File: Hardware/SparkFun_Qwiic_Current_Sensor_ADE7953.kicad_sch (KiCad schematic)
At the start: 45 parts, among them J1 Qwiic_RA, J2 Qwiic_RA, J3 Conn_01x06, J4 Conn_01x02, J5 3.5mm TRRS, J6 Conn_01x02, U1 ADE7953ACPZ, Y1 3.579545MHz

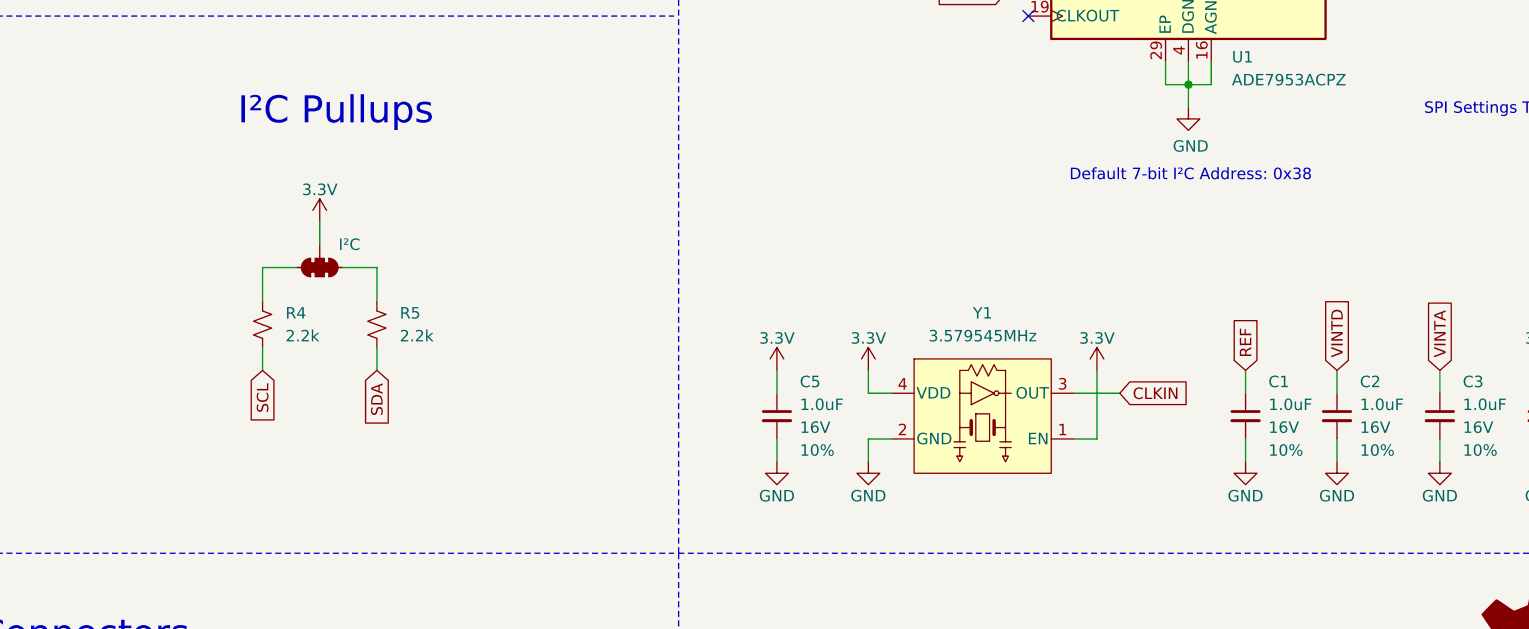
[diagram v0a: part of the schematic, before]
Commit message: Updated PCB based on Design Review II feedback
- Updated schematic I2C labels
- Updated component silkscreens and courtyards
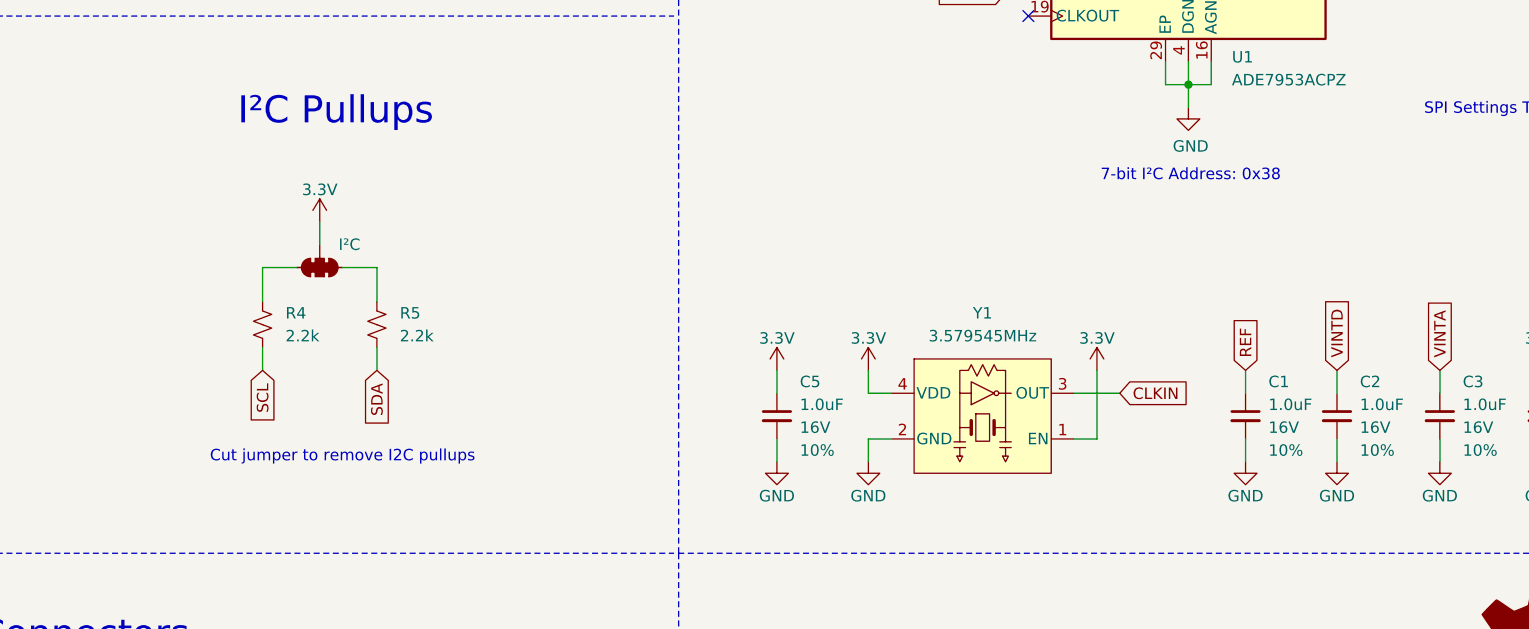
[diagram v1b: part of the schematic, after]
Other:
- note added: "7-bit I²C Address: 0x38"
- note added: "Cut jumper to remove I2C pullups"
- note removed: "Default 7-bit I²C Address: 0x38"
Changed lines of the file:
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@@
 		(title "SparkFun Qwiic Current Sensor ADE7953")
 		(date "2026-05-04")
-		(rev "v01")
+		(rev "v10")
 		(company "SparkFun Electronics")
 		(comment 1 "Designed by: Geoff McIntyre")
@@
 		)
 	)
-	(text "Default 7-bit I²C Address: 0x38\n"
+	(text "7-bit I²C Address: 0x38\n"
 		(exclude_from_sim no)
 		(at 213.614 101.6 0)
@@
 			)
 		)
+	)
+	(text "Cut jumper to remove I2C pullups"
+		(exclude_from_sim no)
+		(at 119.38 132.842 0)
+		(effects
+			(font
+				(size 1.27 1.27)
+				(color 132 132 132 1)
+			)
+		)
